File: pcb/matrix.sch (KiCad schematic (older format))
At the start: 281 parts

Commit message: Add new plate design. Start modfying schematic
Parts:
- removed LS1, LS10, LS11, LS12, LS13, LS14, LS15, LS16, LS17, LS2, LS3, LS4, LS5, LS6, LS7, LS8, LS9: LED, LED_SMD:LED_0805_2012Metric_Pad1.15x1.40mm_HandSolder, symbol Device:LED
- removed MX4_1: MX-LED, ai03-MX_only:MXOnly-1.75U-FLIPPED, symbol ai03-schematic_library:MX-LED
- removed RL1, RL2, RL3, RL4, RL5, RL6, RL7, RS1, RS10, RS11, RS12, RS13, RS14, RS15, RS16, RS17, RS2, RS3, RS4, RS5, RS6, RS7, RS8, RS9: R, Resistor_SMD:R_0805_2012Metric_Pad1.15x1.40mm_HandSolder, symbol Device:R
- added D?: D, Diode_SMD:D_SOD-123, symbol Device:D
- added MX?: MX-LED, ai03-MX_only:MXOnly-1.5U, symbol ai03-schematic_library:MX-LED
- added RL?: R, Resistor_SMD:R_0805_2012Metric_Pad1.15x1.40mm_HandSolder, symbol Device:R
- MX1: value MX-LED -> MX-1.5; footprint ai03-MX_only:MXOnly-1U -> ai03-MX_only:MXOnly-1.5U-NoLED; symbol ai03-schematic_library:MX-LED -> ai03-schematic_library:MX-NoLED
- MX2, MX7: value MX-LED -> MX-1; footprint ai03-MX_only:MXOnly-1U -> ai03-MX_only:MXOnly-1U-NoLED; symbol ai03-schematic_library:MX-LED -> ai03-schematic_library:MX-NoLED
- MX3: value MX-LED -> MX-1.5; footprint ai03-MX_only:MXOnly-1.5U -> ai03-MX_only:MXOnly-1.5U-NoLED; symbol ai03-schematic_library:MX-LED -> ai03-schematic_library:MX-NoLED
- MX4: value MX-LED -> MX-1.75; footprint ai03-MX_only:MXOnly-1.75U -> ai03-MX_only:MXOnly-1.75U-NoLED; symbol ai03-schematic_library:MX-LED -> ai03-schematic_library:MX-NoLED
- MX5: value MX-LED -> MX-2; footprint ai03-MX_only:MXOnly-2.25U -> ai03-MX_only:MXOnly-2U; symbol ai03-schematic_library:MX-LED -> ai03-schematic_library:MX-NoLED
- MX6: value MX-LED -> MX-1.25; footprint ai03-MX_only:MXOnly-1.5U -> ai03-MX_only:MXOnly-1.25U; symbol ai03-schematic_library:MX-LED -> ai03-schematic_library:MX-NoLED
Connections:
- net labels removed: ledGND
- wire segments 854 -> 717
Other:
- note added: "WIN"
- moved on the sheet: D4, D6

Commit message: Remove all leds
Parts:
- removed D?: D, Diode_SMD:D_SOD-123, symbol Device:D
- removed MX?: MX-LED, ai03-MX_only:MXOnly-1.5U, symbol ai03-schematic_library:MX-LED
- removed RL10, RL11, RL12, RL13, RL14, RL15, RL16, RL17, RL18, RL19, RL20, RL21, RL22, RL23, RL24, RL25, RL26, RL27, RL28, RL29, RL30, RL31, RL32, RL33, RL34, RL35, RL36, RL37, RL38, RL39, RL40, RL41, RL42, RL43, RL44, RL45, RL46, RL47, RL48, RL49, RL50, RL51, RL52, RL53, RL54, RL55, RL56, RL57, RL58, RL59, RL60, RL61, RL62, RL63, RL64, RL65, RL66, RL67, RL68, RL69, RL70, RL71, RL72, RL73, RL74, RL75, RL76, RL77, RL78, RL79, RL8, RL80, RL81, RL82, RL9, RL?: R, Resistor_SMD:R_0805_2012Metric_Pad1.15x1.40mm_HandSolder, symbol Device:R
- added D12, D? (x4): D, Diode_SMD:D_SOD-123, symbol Device:D
- added MX12: MX-1.25, ai03-MX_only:MXOnly-1.25U, symbol ai03-schematic_library:MX-NoLED
- added MX? (x4): MX-1, ai03-MX_only:MXOnly-1U-NoLED, symbol ai03-schematic_library:MX-NoLED
- MX10, MX11, MX18, MX19, MX20, MX21, MX22, MX8, MX9: value MX-LED -> MX-1; footprint ai03-MX_only:MXOnly-1U -> ai03-MX_only:MXOnly-1U-NoLED; symbol ai03-schematic_library:MX-LED -> ai03-schematic_library:MX-NoLED
- MX13: renamed from MX12; value MX-LED -> MX-1; footprint ai03-MX_only:MXOnly-1U -> ai03-MX_only:MXOnly-1U-NoLED; symbol ai03-schematic_library:MX-LED -> ai03-schematic_library:MX-NoLED
- MX14: renamed from MX13; value MX-LED -> MX-1; footprint ai03-MX_only:MXOnly-1U -> ai03-MX_only:MXOnly-1U-NoLED; symbol ai03-schematic_library:MX-LED -> ai03-schematic_library:MX-NoLED
- MX15: renamed from MX14; value MX-LED -> MX-1; footprint ai03-MX_only:MXOnly-1U -> ai03-MX_only:MXOnly-1U-NoLED; symbol ai03-schematic_library:MX-LED -> ai03-schematic_library:MX-NoLED
- MX16: renamed from MX15; value MX-LED -> MX-1; footprint ai03-MX_only:MXOnly-1U -> ai03-MX_only:MXOnly-1U-NoLED; symbol ai03-schematic_library:MX-LED -> ai03-schematic_library:MX-NoLED
- MX17: renamed from MX16; value MX-LED -> MX-1; footprint ai03-MX_only:MXOnly-1U -> ai03-MX_only:MXOnly-1U-NoLED; symbol ai03-schematic_library:MX-LED -> ai03-schematic_library:MX-NoLED
- MX18: renamed from MX17; value MX-LED -> MX-1.5; footprint ai03-MX_only:MXOnly-1.5U -> ai03-MX_only:MXOnly-1.5U-NoLED; symbol ai03-schematic_library:MX-LED -> ai03-schematic_library:MX-NoLED
- MX23, MX24, MX25, MX26, MX27, MX29, MX30, MX31, MX32, MX33, MX35, MX36, MX37, MX38, MX39, MX40, MX41, MX42, MX43, MX44, MX46, MX47, MX48, MX49, MX50, MX51, MX52, MX53, MX54, MX55, MX57, MX58, MX59, MX60, MX61, MX62, MX63, MX64, MX65, MX67, MX68, MX69, MX71, MX72, MX73, MX75, MX76, MX77, MX79, MX80, MX81, MX82: footprint ai03-MX_only:MXOnly-1U -> ai03-MX_only:MXOnly-1U-NoLED; symbol ai03-schematic_library:MX-LED -> ai03-schematic_library:MX-NoLED
- MX28: footprint ai03-MX_only:MXOnly-2U-ReversedStabilizers -> ai03-MX_only:MXOnly-2U-ReversedStabilizers-NoLED; symbol ai03-schematic_library:MX-LED -> ai03-schematic_library:MX-NoLED
- MX34: value MX-LED -> MX-LED-NoLED; symbol ai03-schematic_library:MX-LED -> ai03-schematic_library:MX-NoLED
- MX45: footprint ai03-MX_only:MXOnly-2.75U-ReversedStabilizers -> ai03-MX_only:MXOnly-2.75U-ReversedStabilizers-NoLED; symbol ai03-schematic_library:MX-LED -> ai03-schematic_library:MX-NoLED
- MX56: value MX-LED -> MX-1; footprint ai03-MX_only:MXOnly-1.5U -> ai03-MX_only:MXOnly-1U-NoLED; symbol ai03-schematic_library:MX-LED -> ai03-schematic_library:MX-NoLED
- MX66: footprint ai03-MX_only:MXOnly-1.75U -> ai03-MX_only:MXOnly-1.75U-NoLED; symbol ai03-schematic_library:MX-LED -> ai03-schematic_library:MX-NoLED
- MX70: footprint ai03-MX_only:MXOnly-2.25U-ReversedStabilizers -> ai03-MX_only:MXOnly-2.25U-ReversedStabilizers-NoLED; symbol ai03-schematic_library:MX-LED -> ai03-schematic_library:MX-NoLED
- MX74: footprint ai03-MX_only:MXOnly-1.5U -> ai03-MX_only:MXOnly-2U-NoLED; symbol ai03-schematic_library:MX-LED -> ai03-schematic_library:MX-NoLED
- MX78: footprint ai03-MX_only:MXOnly-1U -> ai03-MX_only:MXOnly-1.5U-NoLED; symbol ai03-schematic_library:MX-LED -> ai03-schematic_library:MX-NoLED
- renumbered D12 to D13, D13 to D14, D14 to D15, D15 to D16
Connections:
- net col1: now also MX12.1 (COL)
- net col10: now also MX54.1 (COL), MX55.1 (COL), MX?.1 (COL); no longer MX60.1 (COL), MX61.1 (COL)
- net col11: now also MX60.1 (COL), MX61.1 (COL), MX?.1 (COL); no longer MX65.1 (COL), MX66.1 (COL)
- net col12: now also MX65.1 (COL), MX66.1 (COL); no longer MX70.1 (COL)
- net col13: now also MX70.1 (COL)
- net col6: now also MX?.1 (COL); no longer MX38.1 (COL), MX39.1 (COL)
- net col7: now also MX38.1 (COL), MX39.1 (COL); no longer MX43.1 (COL), MX44.1 (COL)
- net col8: now also MX43.1 (COL), MX44.1 (COL); no longer MX49.1 (COL), MX50.1 (COL)
- net col9: now also MX49.1 (COL), MX50.1 (COL); no longer MX54.1 (COL), MX55.1 (COL)
- net row0: now also D78.1 (K); no longer D77.1 (K)
- net row1: now also D74.1 (K), D79.1 (K); no longer D73.1 (K), D78.1 (K)
- net row2: now also D73.1 (K), D77.1 (K); no longer D74.1 (K), D79.1 (K)
- net row3: now also D81.1 (K); no longer D80.1 (K)
- net row4: now also D80.1 (K); no longer D81.1 (K)
- removed net VCC: MX13.3 (LED), MX14.3 (LED), MX15.3 (LED), MX16.3 (LED), MX17.3 (LED), MX18.3 (LED), MX18.3 (LED), MX19.3 (LED), MX20.3 (LED), MX21.3 (LED), MX22.3 (LED), MX23.3 (LED), MX24.3 (LED), MX25.3 (LED), MX26.3 (LED), MX27.3 (LED), MX28.3 (LED), MX29.3 (LED), MX30.3 (LED), MX31.3 (LED), MX32.3 (LED), MX33.3 (LED), MX34.3 (LED), MX35.3 (LED), MX36.3 (LED), MX37.3 (LED), MX38.3 (LED), MX39.3 (LED), MX40.3 (LED), MX41.3 (LED), MX42.3 (LED), MX43.3 (LED), MX44.3 (LED), MX45.3 (LED), MX46.3 (LED), MX47.3 (LED), MX48.3 (LED), MX49.3 (LED), MX50.3 (LED), MX51.3 (LED), MX52.3 (LED), MX53.3 (LED), MX54.3 (LED), MX55.3 (LED), MX56.3 (LED), MX57.3 (LED), MX58.3 (LED), MX59.3 (LED), MX60.3 (LED), MX61.3 (LED), MX62.3 (LED), MX63.3 (LED), MX64.3 (LED), MX65.3 (LED), MX66.3 (LED), MX67.3 (LED), MX68.3 (LED), MX69.3 (LED), MX70.3 (LED), MX71.3 (LED), MX72.3 (LED), MX73.3 (LED), MX74.3 (LED), MX75.3 (LED), MX76.3 (LED), MX77.3 (LED), MX78.3 (LED), MX79.3 (LED), MX80.3 (LED), MX81.3 (LED), MX82.3 (LED)
- new net: D12.2 (A), MX12.2 (ROW)
- new net: D?.2 (A), MX?.2 (ROW) (x4)
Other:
- note added: "Ctrl\n"
- note added: "F14"
- note added: "F15"
- moved on the sheet: D38, D39, D43, D44, D49, D50, D54, D55, D60, D61, D65, D66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

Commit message: renumber keys
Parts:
- gave numbers to parts that had none: 4
- renumbered MX18 to MX19, MX19 to MX20, MX20 to MX21, MX21 to MX22, MX22 to MX23, MX23 to MX24, MX24 to MX25, MX25 to MX26, MX26 to MX27, MX27 to MX28, MX28 to MX29, MX29 to MX30, MX30 to MX31, MX31 to MX32, MX32 to MX33, MX33 to MX34, MX34 to MX35, MX35 to MX36, MX36 to MX37, MX37 to MX38, MX40 to MX41, MX41 to MX42, MX42 to MX43, MX38 to MX44, MX39 to MX45, MX45 to MX46, MX46 to MX47, MX47 to MX48, MX48 to MX49, MX43 to MX50, MX44 to MX51, MX51 to MX52, MX52 to MX53, MX53 to MX54, MX49 to MX55, MX50 to MX56, MX56 to MX57, MX57 to MX58, MX58 to MX59, MX59 to MX60, MX54 to MX61, MX55 to MX62, MX62 to MX64, MX63 to MX65, MX64 to MX66, MX60 to MX67, MX61 to MX68, MX67 to MX70, MX68 to MX71, MX69 to MX72, MX65 to MX73, MX66 to MX74, MX71 to MX75, MX72 to MX76, MX74 to MX77, MX73 to MX78, MX70 to MX79, MX75 to MX80, MX76 to MX81, MX78 to MX82, MX79 to MX83, MX77 to MX84, MX81 to MX85, MX80 to MX86, MX82 to MX87

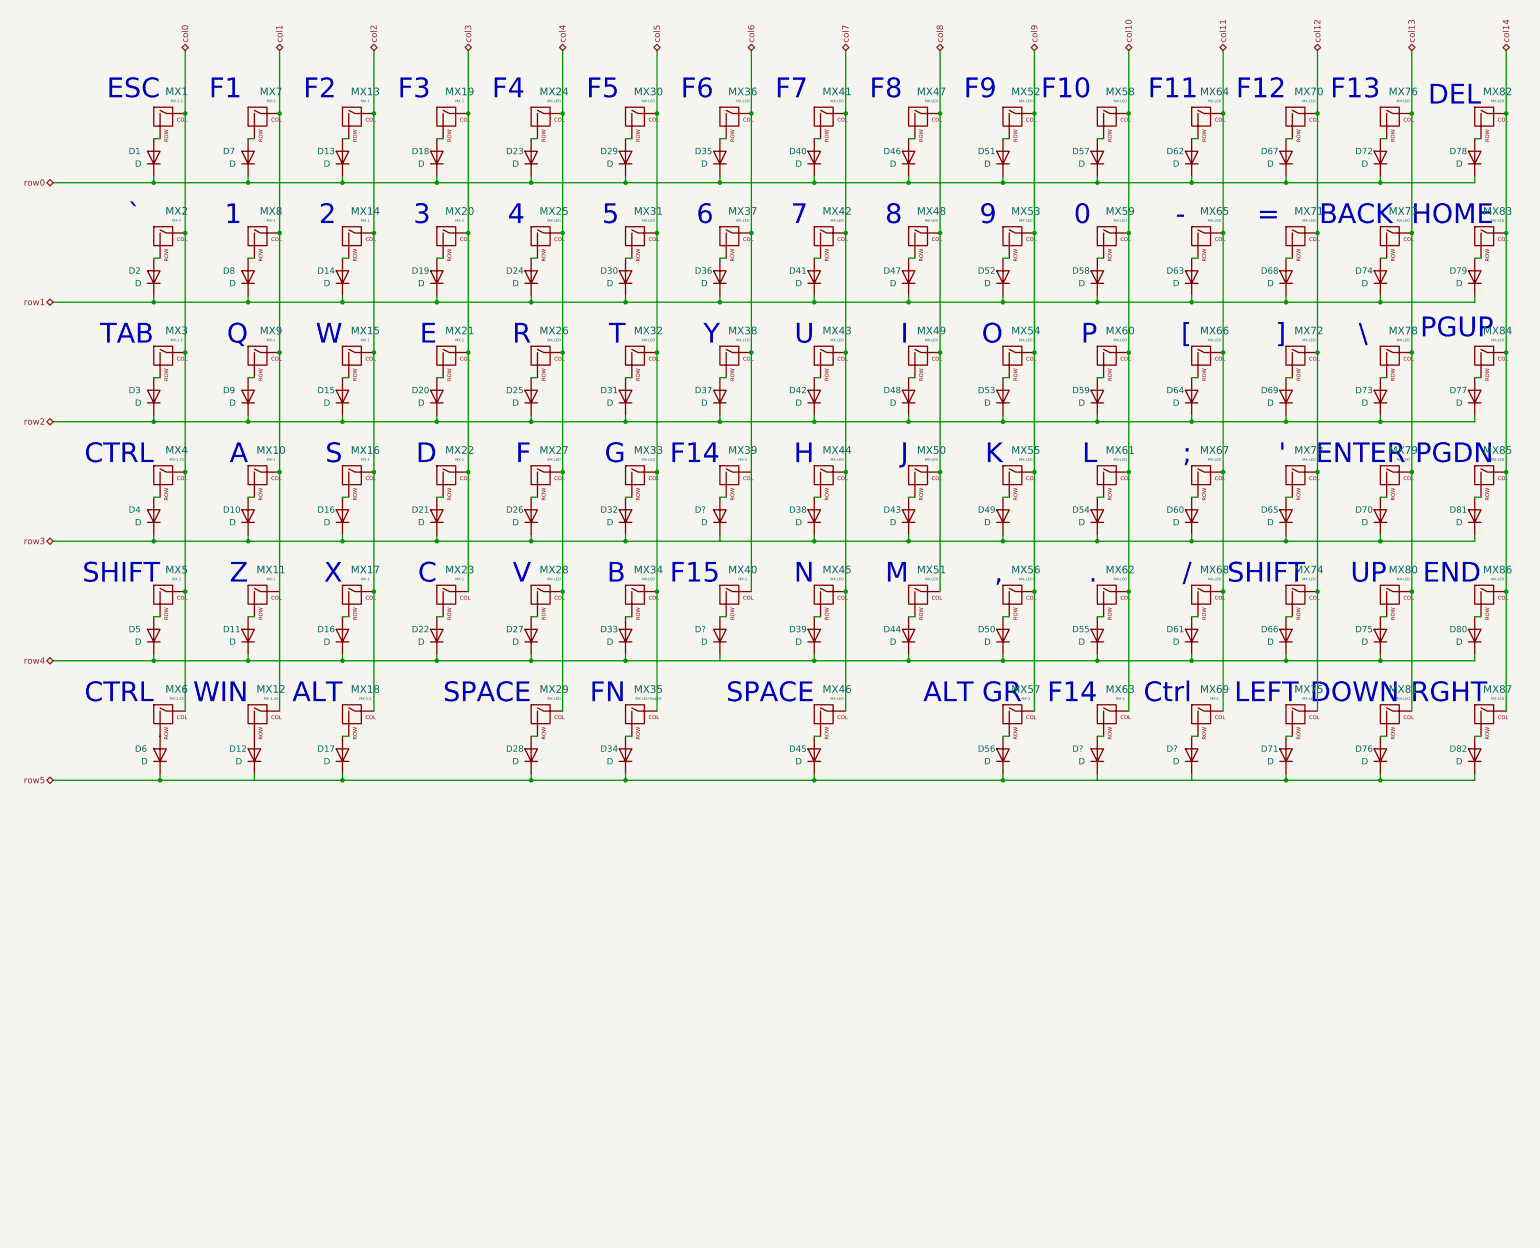
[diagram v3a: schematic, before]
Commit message: Diodes renumbered
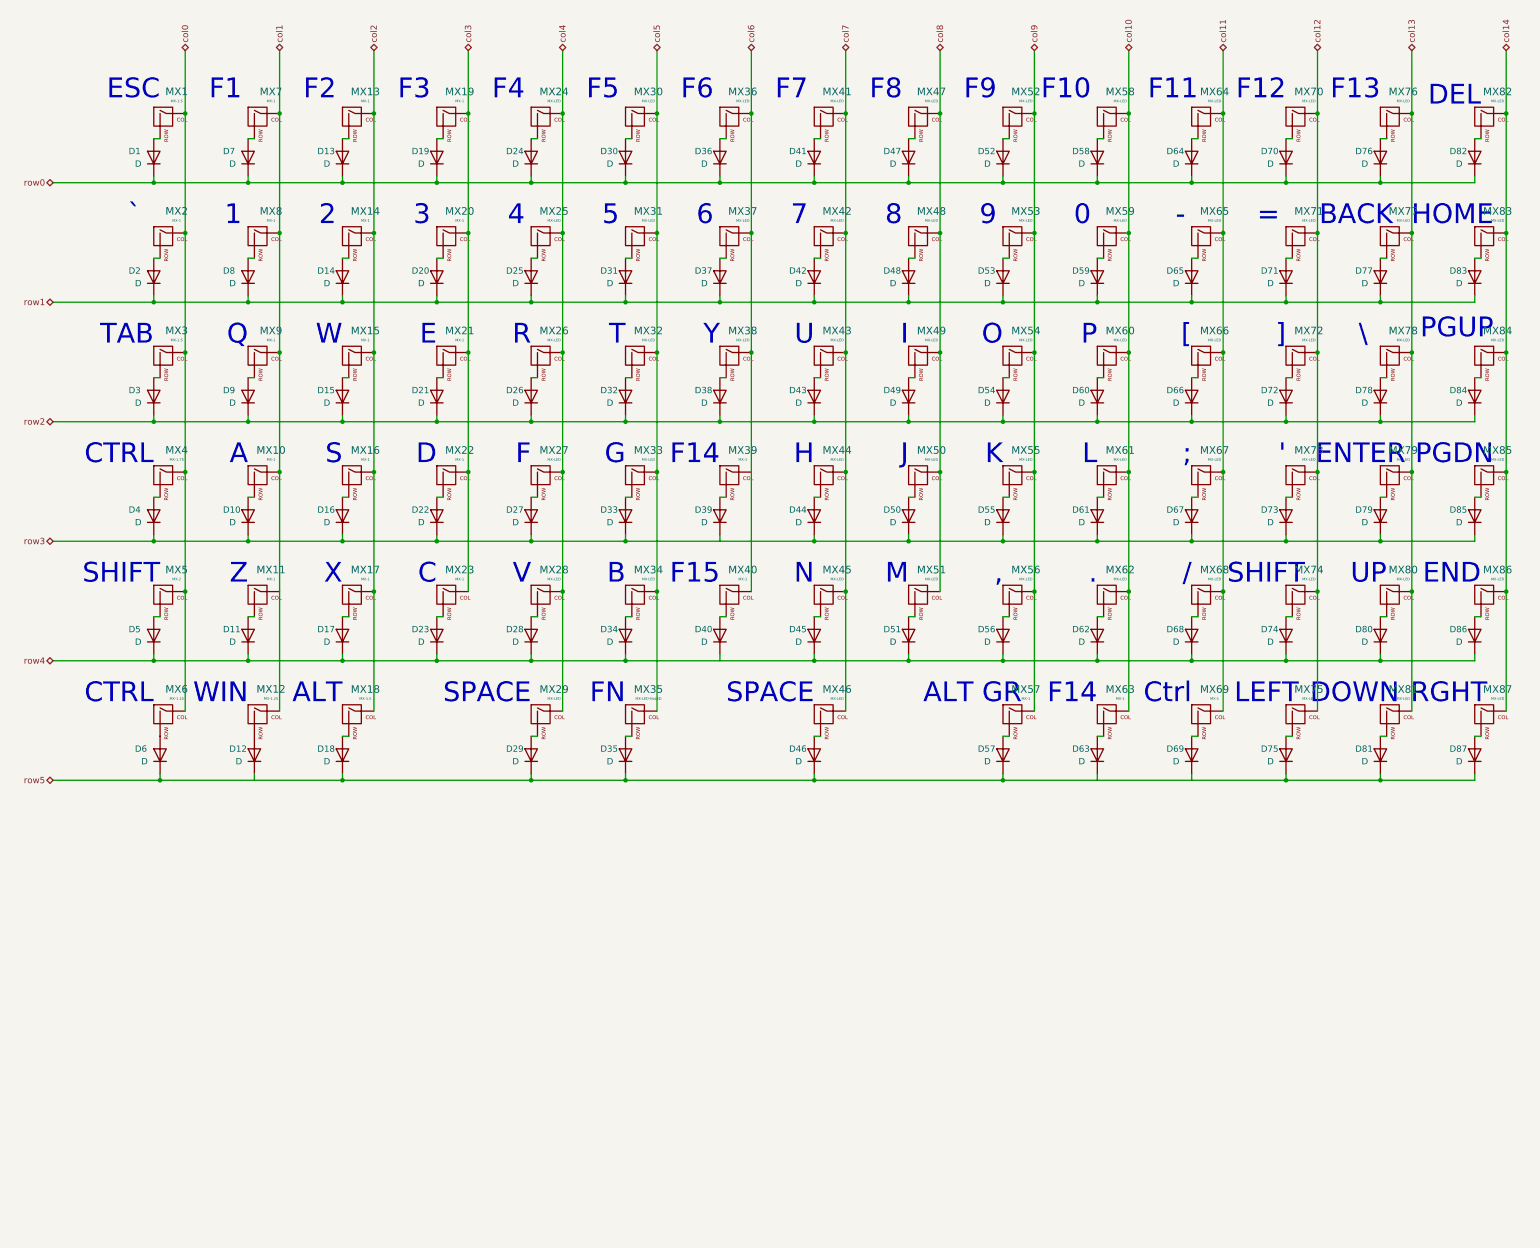
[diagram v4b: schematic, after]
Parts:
- gave numbers to parts that had none: 4
- renumbered D16 to D17, D17 to D18, D18 to D19, D19 to D20, D20 to D21, D21 to D22, D22 to D23, D23 to D24, D24 to D25, D25 to D26, D26 to D27, D27 to D28, D28 to D29, D29 to D30, D30 to D31, D31 to D32, D32 to D33, D33 to D34, D34 to D35, D35 to D36, D36 to D37, D37 to D38, D40 to D41, D41 to D42, D42 to D43, D38 to D44, D39 to D45, D45 to D46, D46 to D47, D47 to D48, D48 to D49, D43 to D50, D44 to D51, D51 to D52, D52 to D53, D53 to D54, D49 to D55, D50 to D56, D56 to D57, D57 to D58, D58 to D59, D59 to D60, D54 to D61, D55 to D62, D62 to D64, D63 to D65, D64 to D66, D60 to D67, D61 to D68, D67 to D70, D68 to D71, D69 to D72, D65 to D73, D66 to D74, D71 to D75, D72 to D76, D74 to D77, D73 to D78, D70 to D79, D75 to D80, D76 to D81, D78 to D82, D79 to D83, D77 to D84, D81 to D85, D80 to D86, D82 to D87
